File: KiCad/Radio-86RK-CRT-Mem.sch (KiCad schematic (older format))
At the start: 20 parts, among them J1 Video, Q1 2N3904, U10 2716/КР573РФ5, U11 2716/КР573РФ5, U13 74198/К155ИР13, U15 7492/К155ИЕ4, U16 7486/К155ЛП5, U17 7474/К155ТМ2, U18 7408/К155ЛИ1, U19 7404/К155ЛН1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

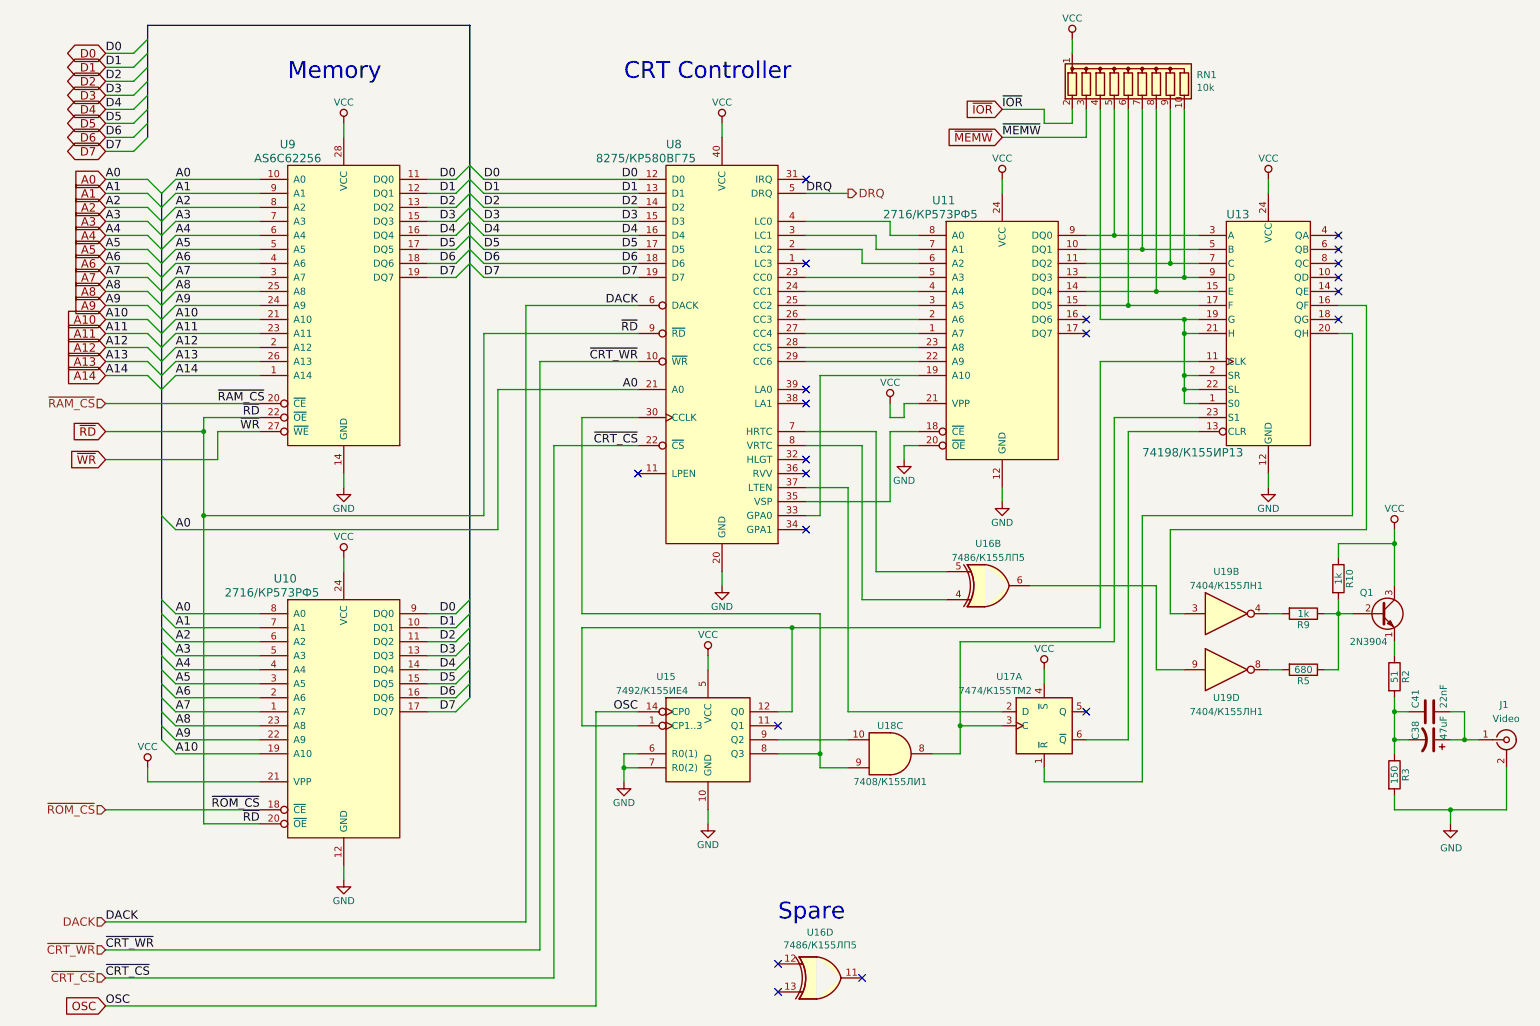
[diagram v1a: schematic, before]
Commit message: Implement inverse video
Signed-off-by: Sergey Kiselev <skiselev@gmail.com>
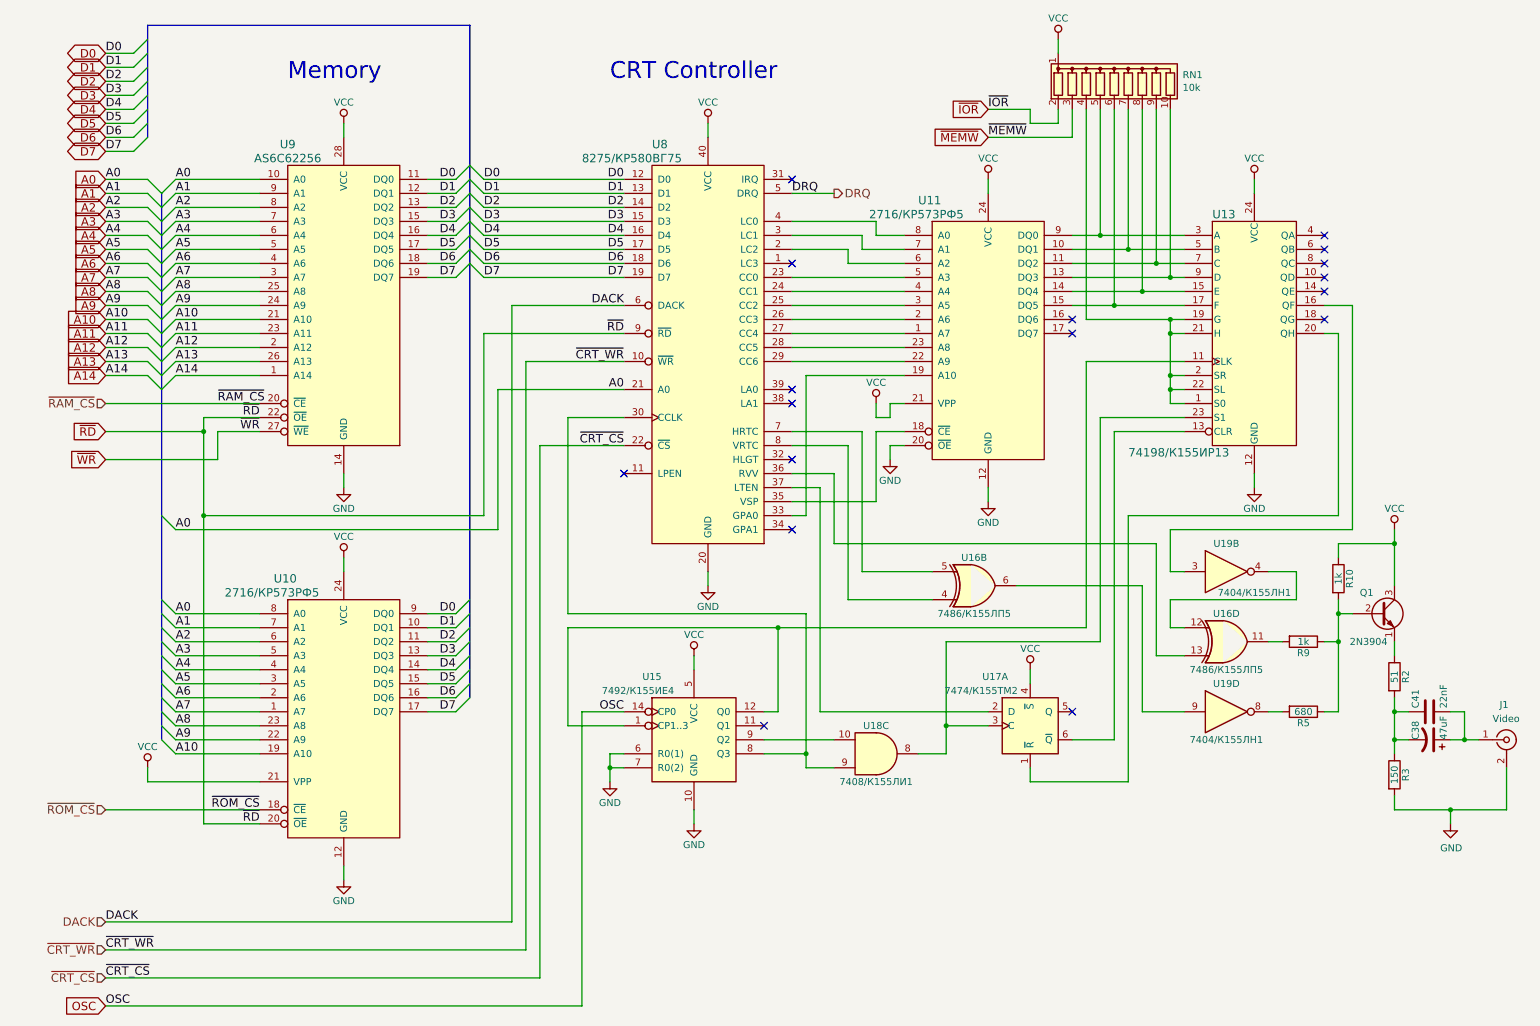
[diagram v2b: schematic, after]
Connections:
- net at U16.11: now also R9.2
- net at U16.12: now also U19.4
- net at U16.13: now also U8.36 (RVV)
- no-connect marks 21 -> 17
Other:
- note removed: "Spare"
- moved on the sheet: R5, R9, RN1, U11, U13, U15, U16B, U16D, U17A, U18C, U19B, U19D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

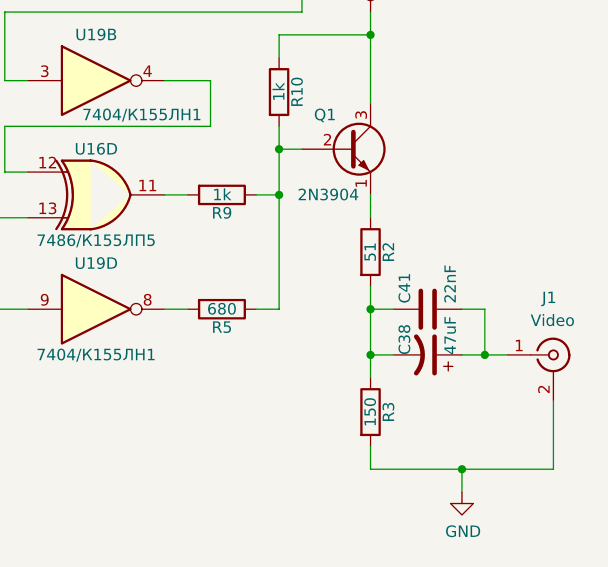
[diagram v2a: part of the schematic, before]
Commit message: Update design files to v1.1
Signed-off-by: Sergey Kiselev <skiselev@gmail.com>
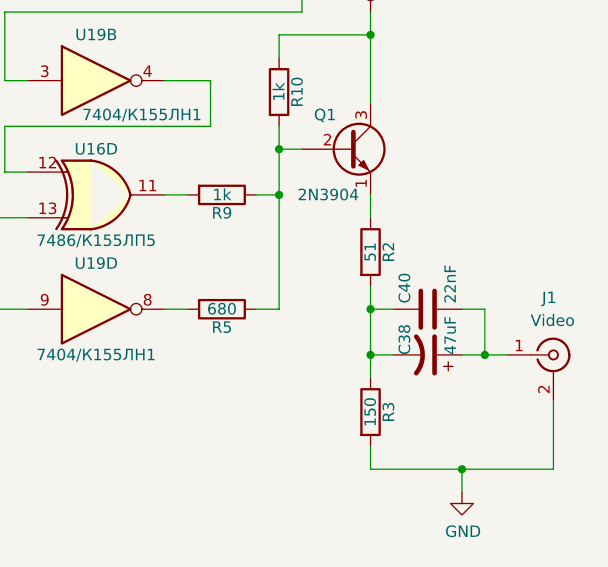
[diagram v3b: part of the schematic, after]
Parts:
- renumbered C41 to C40
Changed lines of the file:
@@
 P 10450 5500
 AR Path="/6203B787" Ref="C?"  Part="1"
-AR Path="/61D307F8/6203B787" Ref="C41"  Part="1"
-F 0 "C41" H 10475 5600 50  0000 L CNN
+AR Path="/61D307F8/6203B787" Ref="C40"  Part="1"
+F 0 "C40" H 10475 5600 50  0000 L CNN
 F 1 "22nF" H 10475 5400 50  0000 L CNN
 F 2 "My_Components:Cap_Cer_508" H 10488 5350 50  0001 C CNN
